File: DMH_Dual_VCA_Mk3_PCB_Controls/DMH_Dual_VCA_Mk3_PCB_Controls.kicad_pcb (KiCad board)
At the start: 2 copper layers, 49 x 121 mm, 38 parts, among them J14 Conn_01x06, J15 Conn_01x08, J16 Conn_01x06, J24 Conn_01x08, SW1 SW_DPDT_3way, SW2 SW_DPDT_OnOffOn_x2, U9 TL074

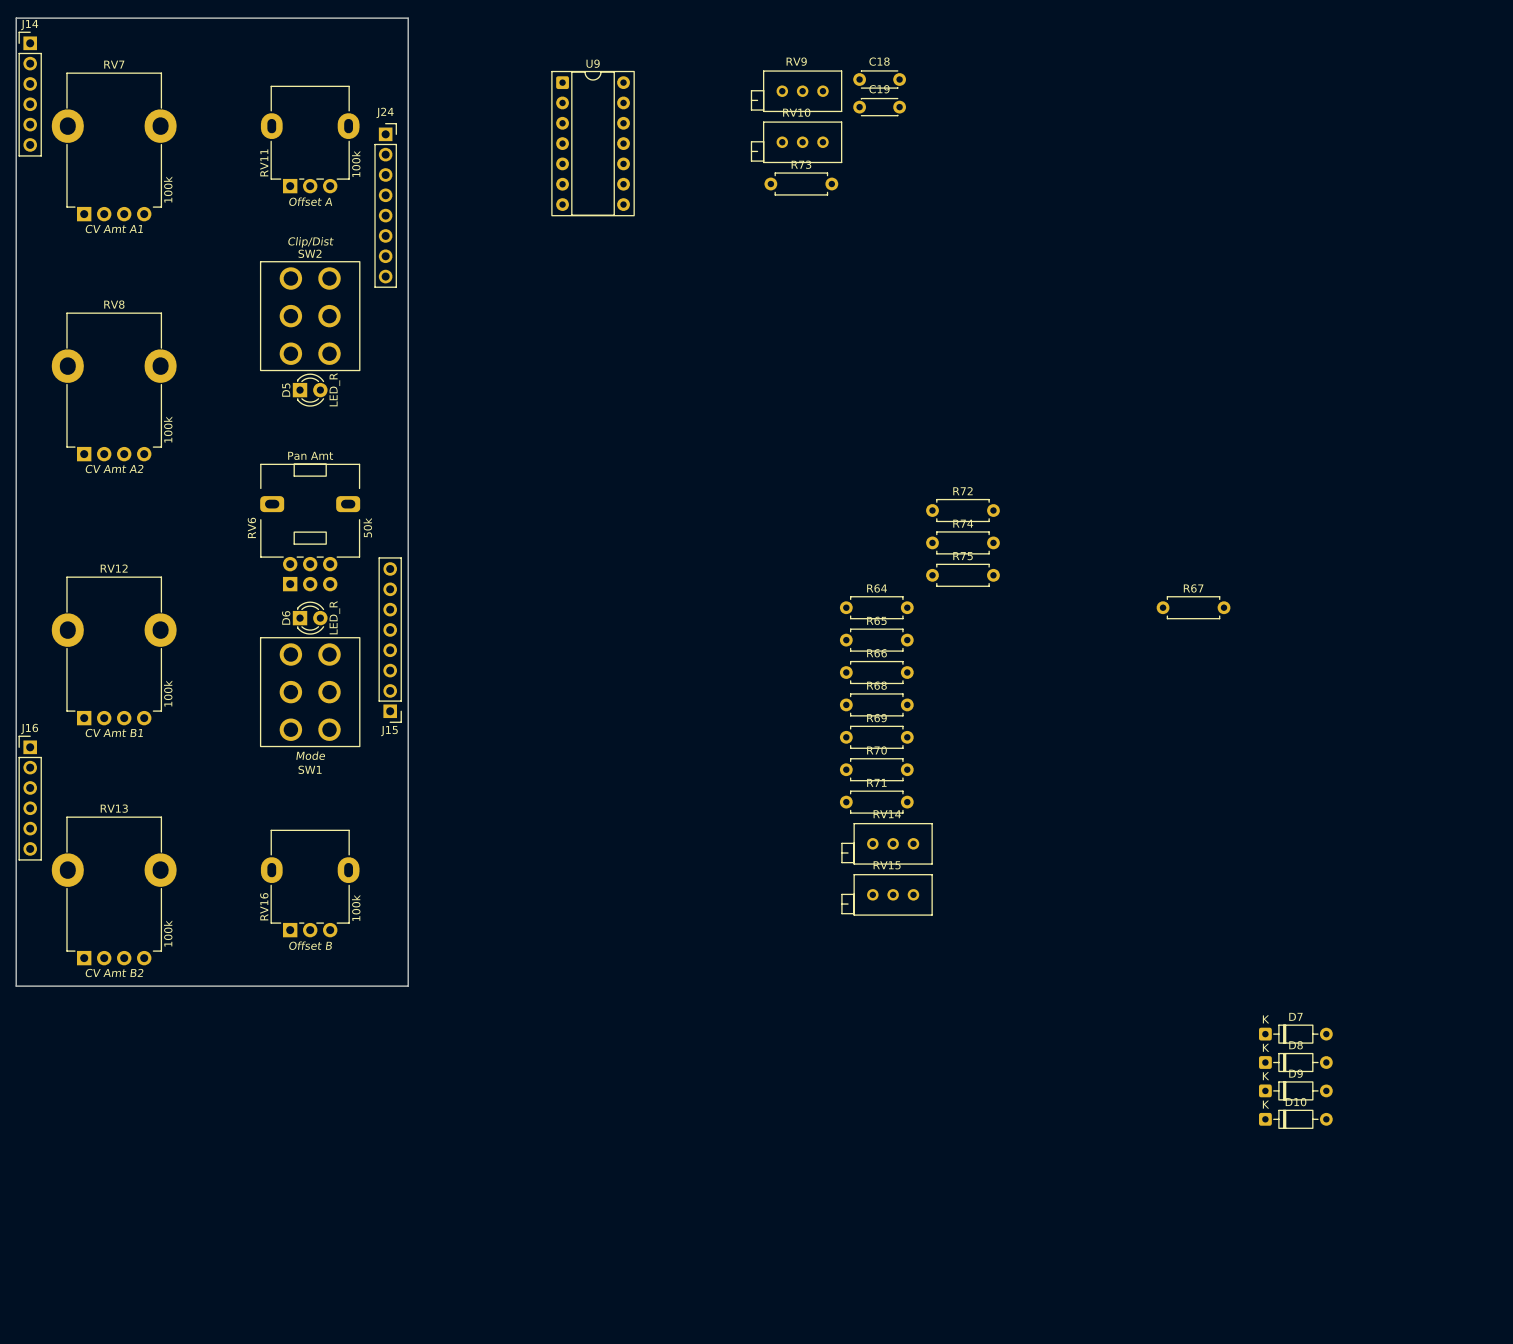
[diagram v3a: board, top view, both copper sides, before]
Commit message: Controls PCB comp placement in progress
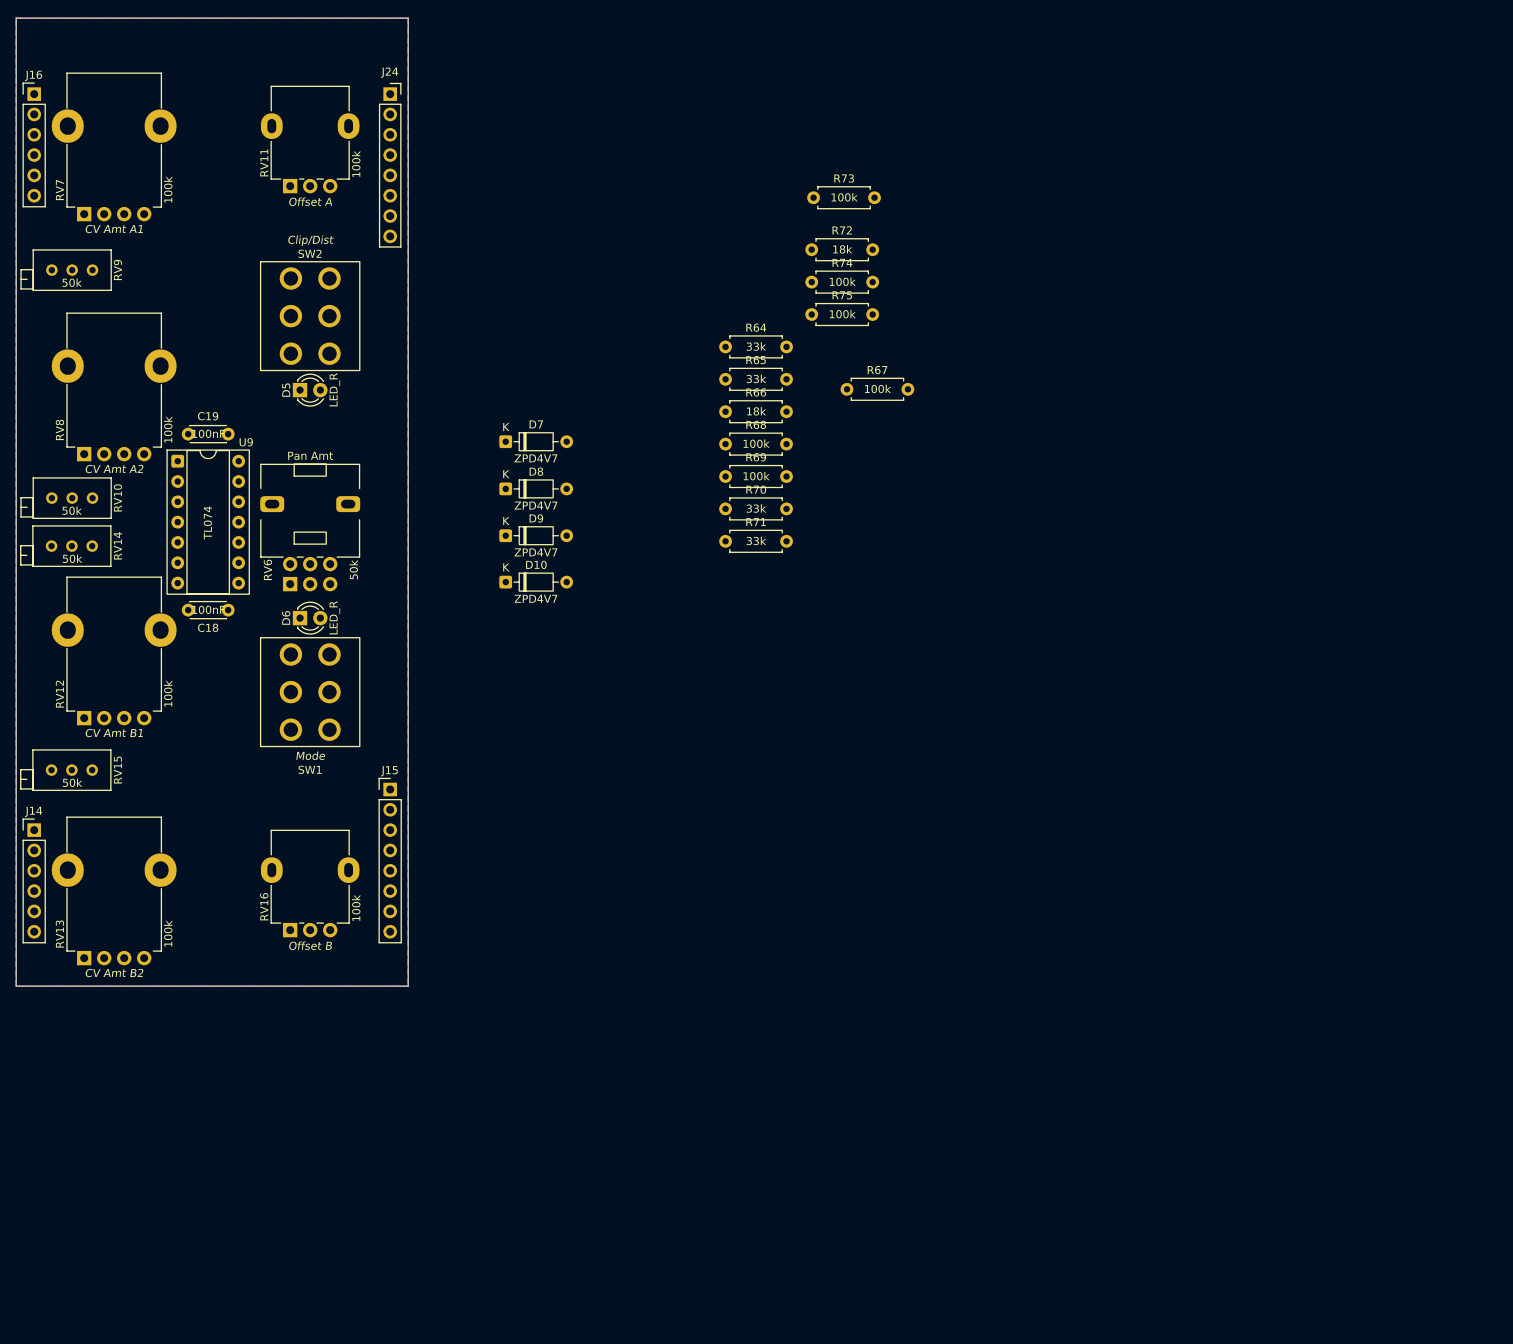
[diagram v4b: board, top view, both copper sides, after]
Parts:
- moved D7 120.4 mm to (111.7, 95.5)
- moved D8 119.0 mm to (111.7, 101.3)
- moved D9 117.6 mm to (111.7, 107.2)
- moved D10 116.3 mm to (111.7, 113.0)
- moved RV14 109.2 mm to (60.0, 108.5)
- moved C18 107.0 mm to (72.0, 116.5)
- moved RV15 103.8 mm to (60.0, 136.5)
- moved RV10 101.6 mm to (60.0, 102.5)
- moved J14 98.4 mm to (52.8, 144.0)
- moved RV9 94.0 mm to (60.0, 74.0)
- moved C19 93.3 mm to (72.0, 94.5)
- moved J16 81.7 mm to (52.8, 52.0)
- moved U9 67.5 mm to (70.7, 97.9)
- moved R67 48.0 mm to (154.3, 88.9)
- moved R64 35.9 mm to (139.2, 83.6)
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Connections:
- J15 pad 1: /Balanced_Offset_c -> /CV_In_PT_c
- J15 pad 2: /Inverted_CV_PT_c -> /CV_PT_Pot_G2_c
- J15 pad 3: /Attenuverted_CV_PT_c -> /CV_PT_Pot_G1_c
- J15 pad 4: /Processed_CV_PT_c -> /Attenuverted_CV_PT_c
- J15 pad 5: /CV_PT_Offset_c -> /Processed_CV_PT_c
- J15 pad 6: /CV_PT_Pot_G1_c -> /Balanced_Offset_c
- J15 pad 7: /CV_PT_Pot_G2_c -> /Inverted_CV_PT_c
- J15 pad 8: /CV_In_PT_c -> /CV_PT_Offset_c
- J16 pad 2: +12V -> +5V
- J16 pad 3: -12V -> -5V
- J16 pad 4: +5V -> -12V
- J16 pad 5: -5V -> +12V
- J24 pad 5: /Clipping/LED_A_pA_c -> /Clipping/LED_A_pK_c
- J24 pad 6: /Clipping/LED_A_pK_c -> /Clipping/LED_A_pA_c
- J24 pad 7: /Clipping/LED_B_pA_c -> /Clipping/LED_B_pK_c
- J24 pad 8: /Clipping/LED_B_pK_c -> /Clipping/LED_B_pA_c
- R64 pad 2: Net-(U9A--) -> Net-(U9D--)
- R65 pad 2: Net-(U9C--) -> Net-(U9A--)
- R71 pad 2: Net-(U9D--) -> Net-(U9C--)
- RV10 pad 1: Net-(U9C--) -> Net-(U9A--)
- RV13 pad 2: Net-(U9D-+) -> Net-(U9C-+)
- RV15 pad 1: Net-(U9D--) -> Net-(U9C--)
- RV7 pad 2: Net-(U9A-+) -> Net-(U9D-+)
- RV8 pad 2: Net-(U9C-+) -> Net-(U9A-+)
- RV9 pad 1: Net-(U9A--) -> Net-(U9D--)
- U9 pad 1: Net-(R68-Pad1) -> Net-(R69-Pad1)
- U9 pad 14: Net-(R75-Pad1) -> Net-(R68-Pad1)
- U9 pad 8: Net-(R69-Pad1) -> Net-(R75-Pad1)
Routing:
- added copper zone on B.Cu, net GND
- added copper zone on F.Cu, net GND
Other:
- board text added: "Mk3.0 - June 2026"
- board text removed: "Mk2.0 - October 2025"

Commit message: Controls PCB comp placement done
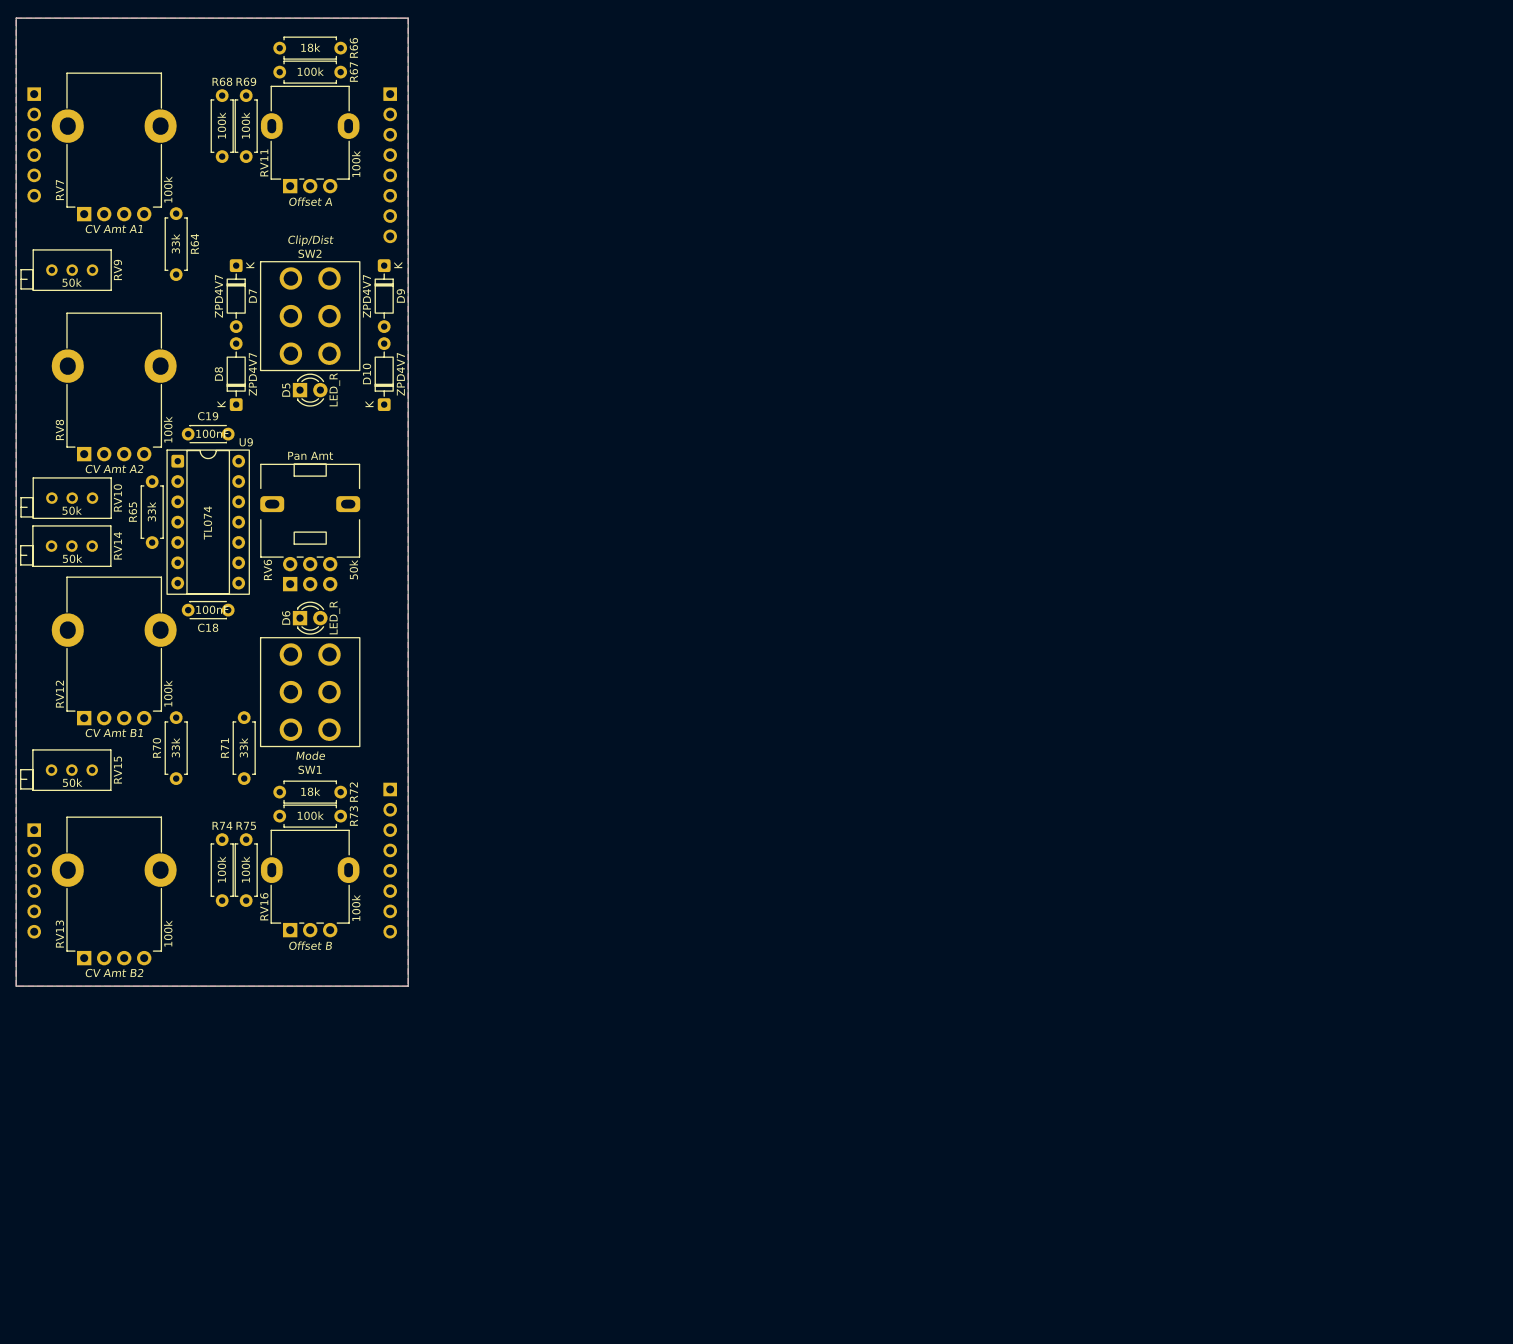
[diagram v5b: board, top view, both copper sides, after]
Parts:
- J14, J16: footprint Connector_PinHeader_2.54mm:PinHeader_1x06_P2.54mm_Vertical -> Connector_PinSocket_2.54mm:PinSocket_1x06_P2.54mm_Vertical; moved to B.Cu
- J15: footprint Connector_PinHeader_2.54mm:PinHeader_1x08_P2.54mm_Vertical -> Connector_PinSocket_2.54mm:PinSocket_1x08_P2.54mm_Vertical; moved to B.Cu
- J24: moved to B.Cu
- moved R74 101.4 mm to (76.2, 145.2), turned to -90 degrees
- moved R73 97.3 mm to (91.1, 142.2), turned to 180 degrees
- moved R75 96.5 mm to (79.2, 145.2), turned to -90 degrees
- moved R72 89.8 mm to (91.1, 139.2), turned to 180 degrees
- moved R70 76.5 mm to (70.5, 137.6), turned to 90 degrees
- moved R67 74.7 mm to (91.1, 49.2), turned to 180 degrees
- moved R65 74.5 mm to (67.5, 108.1), turned to 90 degrees
- moved R68 72.5 mm to (76.2, 59.8), turned to 90 degrees
- moved R69 72.0 mm to (79.2, 59.8), turned to 90 degrees
- moved R64 70.7 mm to (70.5, 66.9), turned to -90 degrees
- moved R71 67.1 mm to (79.0, 137.6), turned to 90 degrees
- moved R66 66.2 mm to (91.1, 46.2), turned to 180 degrees
- moved D7 40.2 mm to (78.0, 73.4), turned to -90 degrees
- moved D9 37.0 mm to (96.5, 73.4), turned to -90 degrees
- moved D8 35.3 mm to (78.0, 90.8), turned to 90 degrees
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
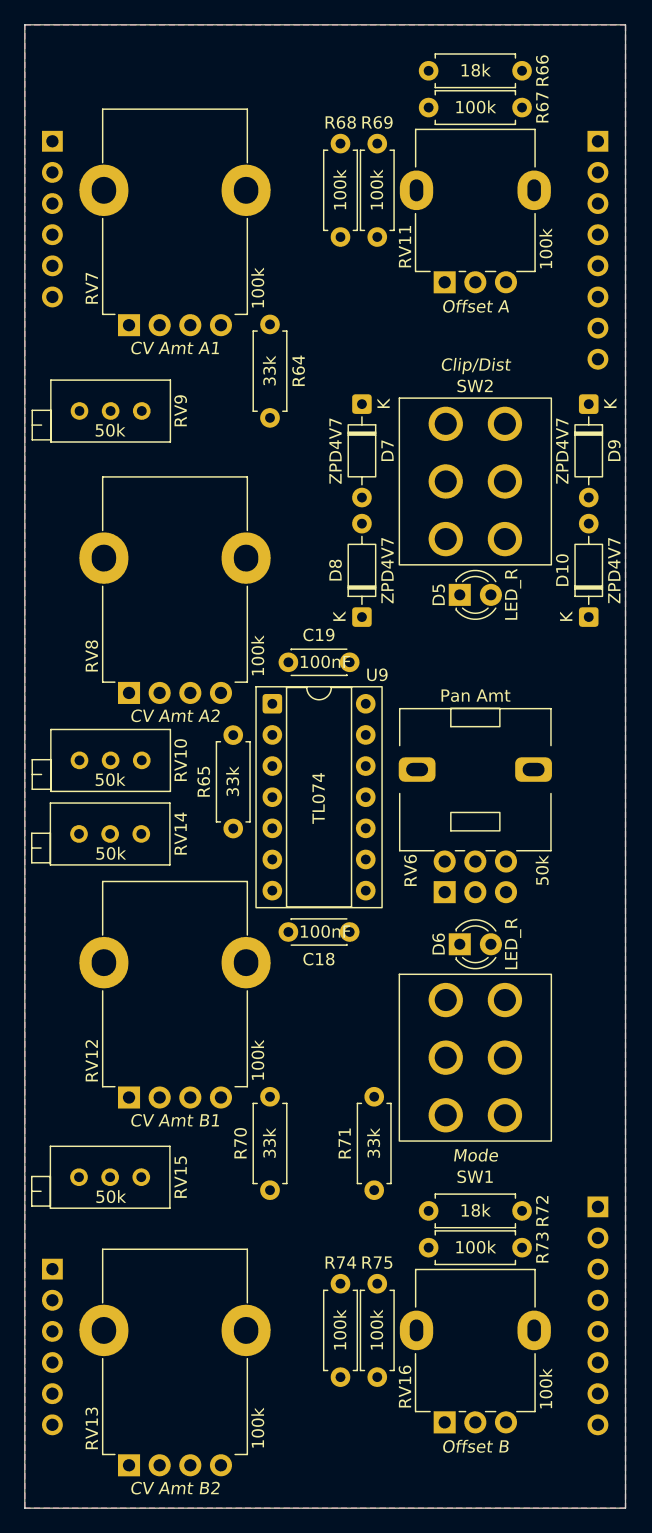
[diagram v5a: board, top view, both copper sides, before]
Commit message: Controls PCB routing done
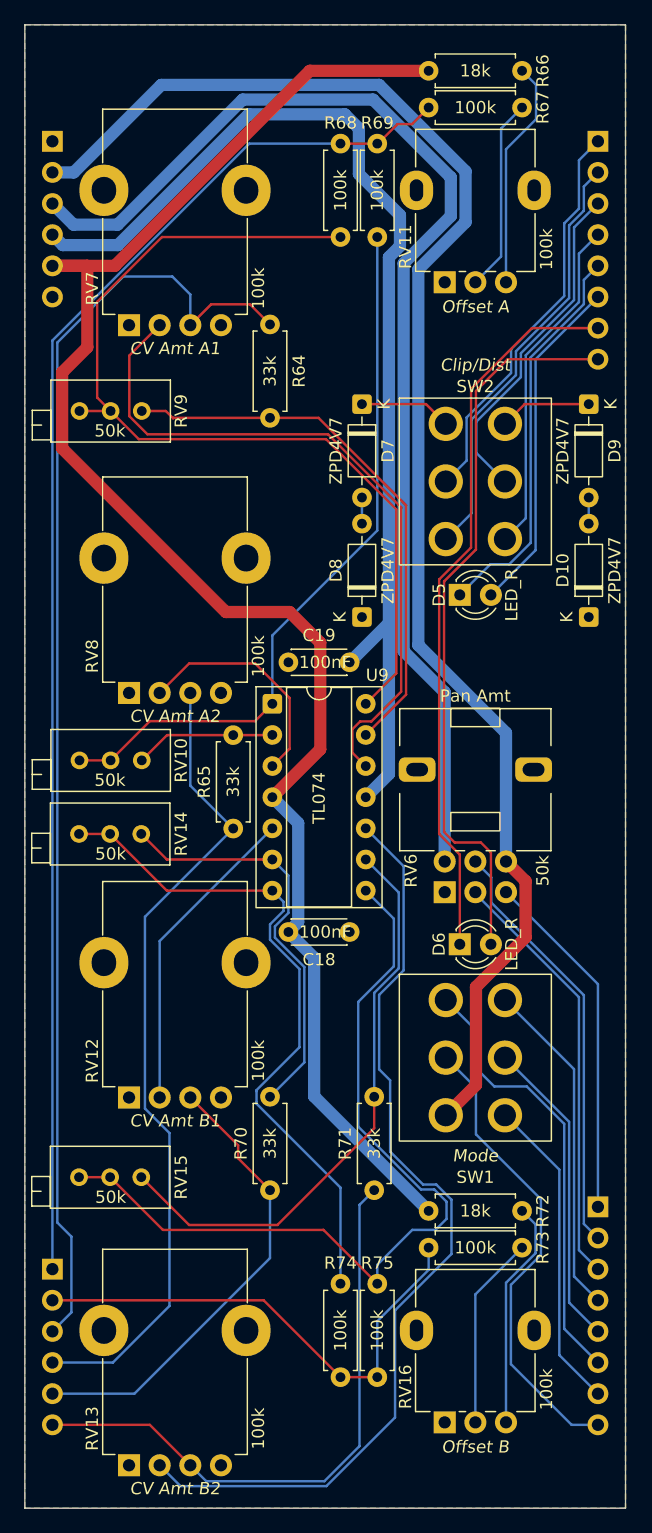
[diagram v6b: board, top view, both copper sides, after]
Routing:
- net +12V: track 0.00 -> 137.4 mm
- net +5V: track 0.00 -> 124.5 mm
- net /Processed_CV_A_c: track 0.00 -> 114.3 mm
- net /CV_In_A1_c: track 0.00 -> 105.9 mm
- net -5V: track 0.00 -> 98.9 mm
- net -12V: track 0.00 -> 91.9 mm
- net Net-(R68-Pad1): track 0.00 -> 77.4 mm
- net Net-(U9C-+): track 0.00 -> 77.4 mm
- net Net-(R75-Pad1): track 0.00 -> 69.2 mm
- net /CV_In_A2_c: track 0.00 -> 66.7 mm
- net /Clipping/LED_B_pA_c: track 0.00 -> 60.1 mm
- net /Clipping/LED_B_pK_c: track 0.00 -> 59.5 mm
- net Net-(R69-Pad1): track 0.00 -> 59.3 mm
- net Net-(U9D-+): track 0.00 -> 57.5 mm
- net Net-(R74-Pad1): track 0.00 -> 55.9 mm
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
